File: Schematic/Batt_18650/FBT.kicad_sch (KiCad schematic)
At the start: 17 parts, among them J1 TRRS Connector 3.5, J2 Conn_01x04, SW1 SW_SPDT

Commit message: work on PCBs, logos, and case
did more work on 18650 battery model
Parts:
- removed J2: Conn_01x04, Connector_JST:JST_PH_S4B-PH-K_1x04_P2.00mm_Horizontal, symbol Connector_Generic:Conn_01x04
- added BT-2: Battery anode, Connector_PinHeader_2.54mm:PinHeader_1x01_P2.54mm_Vertical, symbol Connector_Generic:Conn_01x01
- added J2: TRRS Connector 3.5, My_Library:PJ-320A, symbol Connector_Audio:AudioJack4
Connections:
- net ESP32_3V3: now also J2.T
- net GND: now also BT-2.1 (Pin_1), J2.S
- net SCL_1: now also J2.R2
- net SDA_1: now also J2.R1
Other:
- note added: "The GY-27X must be connected to the BMI's 3v3 output so that its logic levels are 3v3. Connecting it to 5v is OK for the GY-273, but the GY-271 will alter i2c logic levels to output 5V, which may hurt the BMI160 Depending on the IMU board, it may not have a 5v tolerant input and instead may need to tap into the 3v3 one. I made the 3v3 input the default one for the sake of versatility."
- note removed: "The GY-27X must be connected to the BMI's 3v3 output so that its logic levels are 3v3. Connecting it to 5v is OK for the GY-273, but the GY-271 will alter i2c logic levels to output 5V, which may hurt the BMI160 Depending on the IMU board, it may not have a 5v tolerant input and instead may need to tap into the 3v3 one."
- moved on the sheet: J1, MCU1

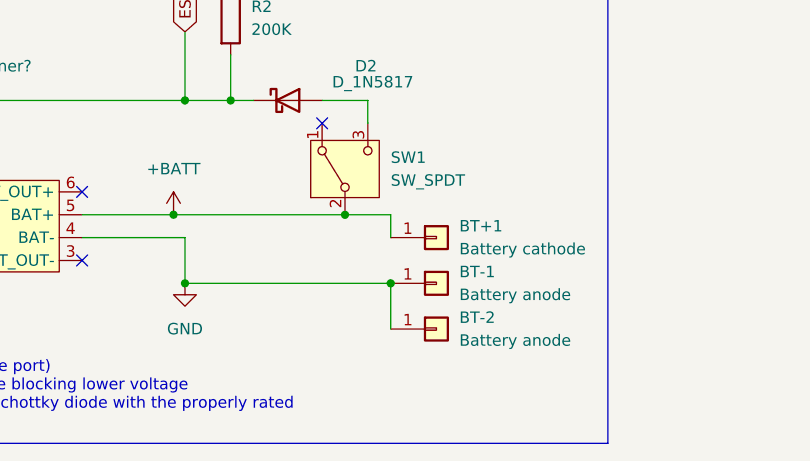
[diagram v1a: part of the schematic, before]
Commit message: Work on 18650 PCB
It's done, but I may re-do this one to flip the ESP32 sideways...
(I then proceeded to work on the sideways version)
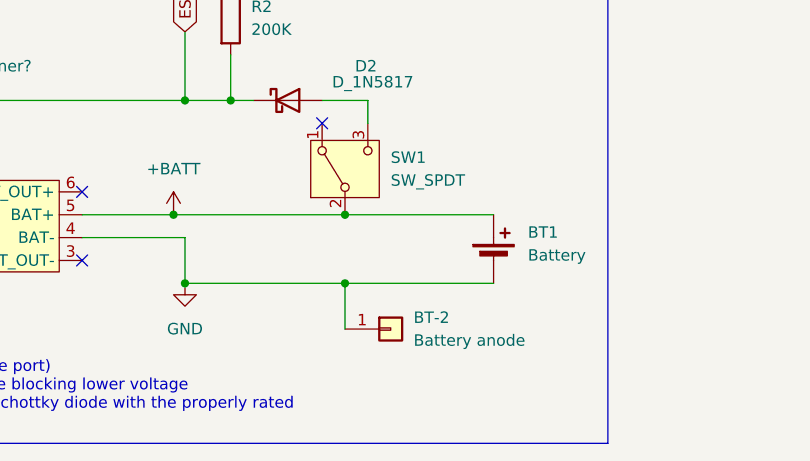
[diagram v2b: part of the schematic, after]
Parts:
- removed BT+1: Battery cathode, Connector_PinHeader_2.54mm:PinHeader_1x01_P2.54mm_Vertical, symbol Connector_Generic:Conn_01x01
- removed BT-1: Battery anode, Connector_PinHeader_2.54mm:PinHeader_1x01_P2.54mm_Vertical, symbol Connector_Generic:Conn_01x01
- added BT1: Battery, Connector_PinHeader_2.54mm:PinHeader_1x02_P2.54mm_Vertical, symbol Device:Battery_Cell
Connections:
- net +BATT: now also BT1.1 (+)
- net GND: now also BT1.2 (-)
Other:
- moved on the sheet: BT-2
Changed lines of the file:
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@@
-	)
-	(junction
-		(at 259.08 140.97)
-		(diameter 0)
-		(color 0 0 0 0)
 	)
 	(junction
@@
 	)
 	(junction
+		(at 254 140.97)
+		(diameter 0)
+		(color 0 0 0 0)
+	)
+	(junction
 		(at 236.22 140.97)
 		(diameter 0)
@@
 	(wire
 		(pts
-			(xy 259.08 135.89) (xy 259.08 133.35)
-		)
-		(stroke
-			(width 0)
-			(type default)
-		)
-	)
-	(wire
-		(pts
 			(xy 261.62 34.29) (xy 261.62 41.91)
 		)
@@
 	(wire
 		(pts
+			(xy 254 140.97) (xy 270.51 140.97)
+		)
+		(stroke
+			(width 0)
+			(type default)
+		)
+	)
+	(wire
+		(pts
 			(xy 227.33 68.58) (xy 229.87 68.58)
 		)
@@
 	(wire
 		(pts
-			(xy 259.08 140.97) (xy 259.08 146.05)
-		)
-		(stroke
-			(width 0)
-			(type default)
-		)
-	)
-	(wire
-		(pts
 			(xy 241.3 106.68) (xy 241.3 107.95)
 		)
@@
 	(wire
 		(pts
-			(xy 254 133.35) (xy 259.08 133.35)
+			(xy 254 133.35) (xy 270.51 133.35)
 		)
 		(stroke
@@
 	(wire
 		(pts
-			(xy 236.22 140.97) (xy 259.08 140.97)
+			(xy 236.22 140.97) (xy 254 140.97)
+		)
+		(stroke
+			(width 0)
+			(type default)
+		)
+	)
+	(wire
+		(pts
+			(xy 254 140.97) (xy 254 146.05)
 		)
 		(stroke
@@
 	(symbol
 		(lib_id "Connector_Generic:Conn_01x01")
-		(at 264.16 146.05 0)
+		(at 259.08 146.05 0)
 		(unit 1)
 		(exclude_from_sim no)
@@
 		(fields_autoplaced yes)
 		(property "Reference" "BT-2"
-			(at 266.7 144.7799 0)
+			(at 261.62 144.7799 0)
 			(effects
 				(font
@@
 		)
 		(property "Value" "Battery anode"
-			(at 266.7 147.3199 0)
+			(at 261.62 147.3199 0)
 			(effects
 				(font
@@
 		)
 		(property "Footprint" "Connector_PinHeader_2.54mm:PinHeader_1x01_P2.54mm_Vertical"
-			(at 264.16 146.05 0)
+			(at 259.08 146.05 0)
 			(effects
 				(font
@@
 		)
 		(property "Datasheet" "~"
-			(at 264.16 146.05 0)
+			(at 259.08 146.05 0)
 			(effects
 				(font
@@
 		)
 		(property "Description" "Generic connector, single row, 01x01, script generated (kicad-library-utils/schlib/autogen/connector/)"
-			(at 264.16 146.05 0)
+			(at 259.08 146.05 0)
 			(effects
 				(font
@@
 				(path "/b59d625c-f89d-4113-8c77-569da8af0dbc"
 					(reference "#PWR01")
+					(unit 1)
+				)
+			)
+		)
+	)
+	(symbol
+		(lib_id "Device:Battery_Cell")
+		(at 270.51 138.43 0)
+		(unit 1)
+		(exclude_from_sim no)
+		(in_bom yes)
+		(on_board yes)
+		(dnp no)
+		(fields_autoplaced yes)
+		(property "Reference" "BT1"
+			(at 274.32 135.3184 0)
+			(effects
+				(font
+					(size 1.27 1.27)
+				)
+				(justify left)
+			)
+		)
+		(property "Value" "Battery"
+			(at 274.32 137.8584 0)
+			(effects
+				(font
+					(size 1.27 1.27)
+				)
+				(justify left)
+			)
+		)
+		(property "Footprint" "Connector_PinHeader_2.54mm:PinHeader_1x02_P2.54mm_Vertical"
+			(at 270.51 136.906 90)
+			(effects
+				(font
+					(size 1.27 1.27)
+				)
+				(hide yes)
+			)
+		)
+		(property "Datasheet" "~"
+			(at 270.51 136.906 90)
+			(effects
+				(font
+					(size 1.27 1.27)
+				)
+				(hide yes)
+			)
+		)
+		(property "Description" "Single-cell battery"
+			(at 270.51 138.43 0)
+			(effects
+				(font
+					(size 1.27 1.27)
+				)
+				(hide yes)
+			)
+		)
+		(pin "2"
+		)
+		(pin "1"
+		)
+		(instances
+			(project "FBT"
+				(path "/b59d625c-f89d-4113-8c77-569da8af0dbc"
+					(reference "BT1")
 					(unit 1)
 				)
@@
 	)
 	(symbol
-		(lib_id "Connector_Generic:Conn_01x01")
-		(at 264.16 135.89 0)
-		(unit 1)
-		(exclude_from_sim no)
-		(in_bom yes)
-		(on_board yes)
-		(dnp no)
-		(fields_autoplaced yes)
-		(property "Reference" "BT+1"
-			(at 266.7 134.6199 0)
-			(effects
-				(font
-					(size 1.27 1.27)
-				)
-				(justify left)
-			)
-		)
-		(property "Value" "Battery cathode"
-			(at 266.7 137.1599 0)
-			(effects
-				(font
-					(size 1.27 1.27)
-				)
-				(justify left)
-			)
-		)
-		(property "Footprint" "Connector_PinHeader_2.54mm:PinHeader_1x01_P2.54mm_Vertical"
-			(at 264.16 135.89 0)
-			(effects
-				(font
-					(size 1.27 1.27)
-				)
-				(hide yes)
-			)
-		)
-		(property "Datasheet" "~"
-			(at 264.16 135.89 0)
-			(effects
-				(font
-					(size 1.27 1.27)
-				)
-				(hide yes)
-			)
-		)
-		(property "Description" "Generic connector, single row, 01x01, script generated (kicad-library-utils/schlib/autogen/connector/)"
-			(at 264.16 135.89 0)
-			(effects
-				(font
-					(size 1.27 1.27)
-				)
-				(hide yes)
-			)
-		)
-		(pin "1"
-		)
-		(instances
-			(project "FBT"
-				(path "/b59d625c-f89d-4113-8c77-569da8af0dbc"
-					(reference "BT+1")
-					(unit 1)
-				)
-			)
-		)
-	)
-	(symbol
 		(lib_id "My_Library:GY-BMI160")
 		(at 240.03 44.45 0)
@@
 					(unit 1)
 				)
-			)
-		)
-	)
-	(symbol
-		(lib_id "Connector_Generic:Conn_01x01")
-		(at 264.16 140.97 0)
-		(unit 1)
-		(exclude_from_sim no)
-		(in_bom yes)
-		(on_board yes)
-		(dnp no)
-		(fields_autoplaced yes)
-		(property "Reference" "BT-1"
-			(at 266.7 139.6999 0)
-			(effects
-				(font
-					(size 1.27 1.27)
-				)
-				(justify left)
-			)
-		)
-		(property "Value" "Battery anode"
-			(at 266.7 142.2399 0)
-			(effects
-				(font
-					(size 1.27 1.27)
-				)
-				(justify left)
-			)
-		)
-		(property "Footprint" "Connector_PinHeader_2.54mm:PinHeader_1x01_P2.54mm_Vertical"
-			(at 264.16 140.97 0)
-			(effects
-				(font
-					(size 1.27 1.27)
-				)
-				(hide yes)
-			)
-		)
-		(property "Datasheet" "~"
-			(at 264.16 140.97 0)
-			(effects
-				(font
-					(size 1.27 1.27)
-				)
-				(hide yes)
-			)
-		)
-		(property "Description" "Generic connector, single row, 01x01, script generated (kicad-library-utils/schlib/autogen/connector/)"
-			(at 264.16 140.97 0)
-			(effects
-				(font
-					(size 1.27 1.27)
-				)
-				(hide yes)
-			)
-		)
-		(pin "1"
-		)
-		(instances
-			(project "FBT"
-				(path "/b59d625c-f89d-4113-8c77-569da8af0dbc"
-					(reference "BT-1")
-					(unit 1)
-				)

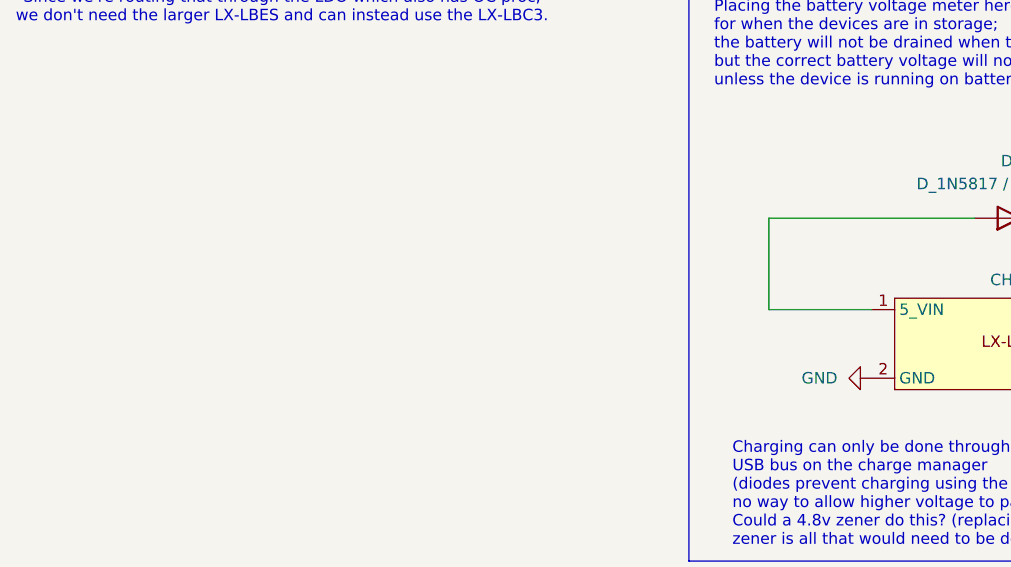
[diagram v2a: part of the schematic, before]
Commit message: work on correcting Ms. Tracker
it has to be a little bit bigger unfortunately...
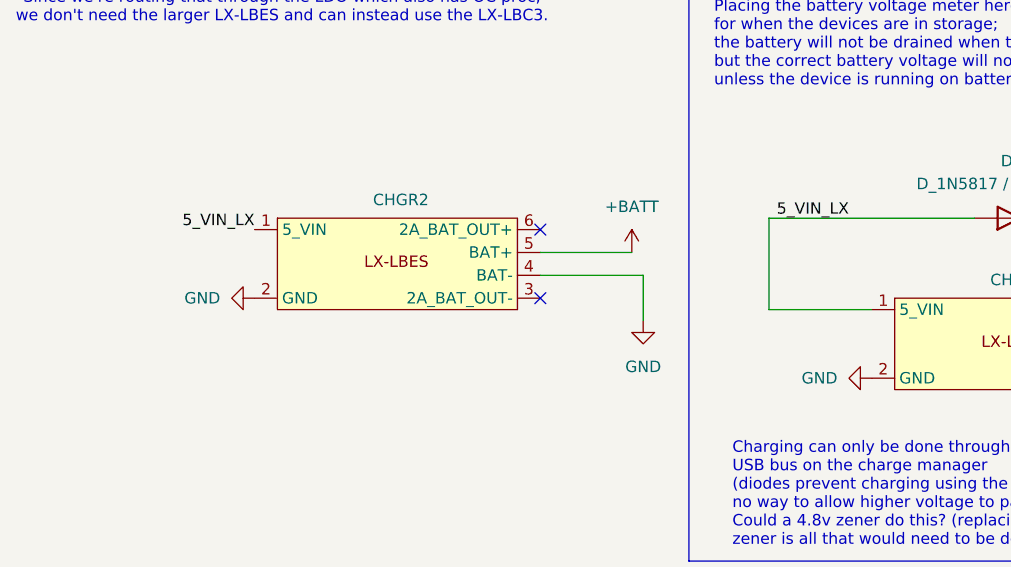
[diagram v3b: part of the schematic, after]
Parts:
- added CHGR2: ~, My_Library:LX-LBES-Big, symbol My_Library:LX-LBES
- MCU1: footprint Espressif:ESP32-C3-SuperMini_PLUS -> Espressif:ESP32-C3-Mini-V1
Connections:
- net +BATT: now also CHGR2.5 (BAT+)
- net GND: now also CHGR2.2 (GND), CHGR2.4 (BAT-)
- net 5_VIN_LX: now reaches CHGR1.1 (5_VIN), D1.2 (A)
- net 5_VIN_LX: now also CHGR2.1 (5_VIN)
- no-connect marks 25 -> 27

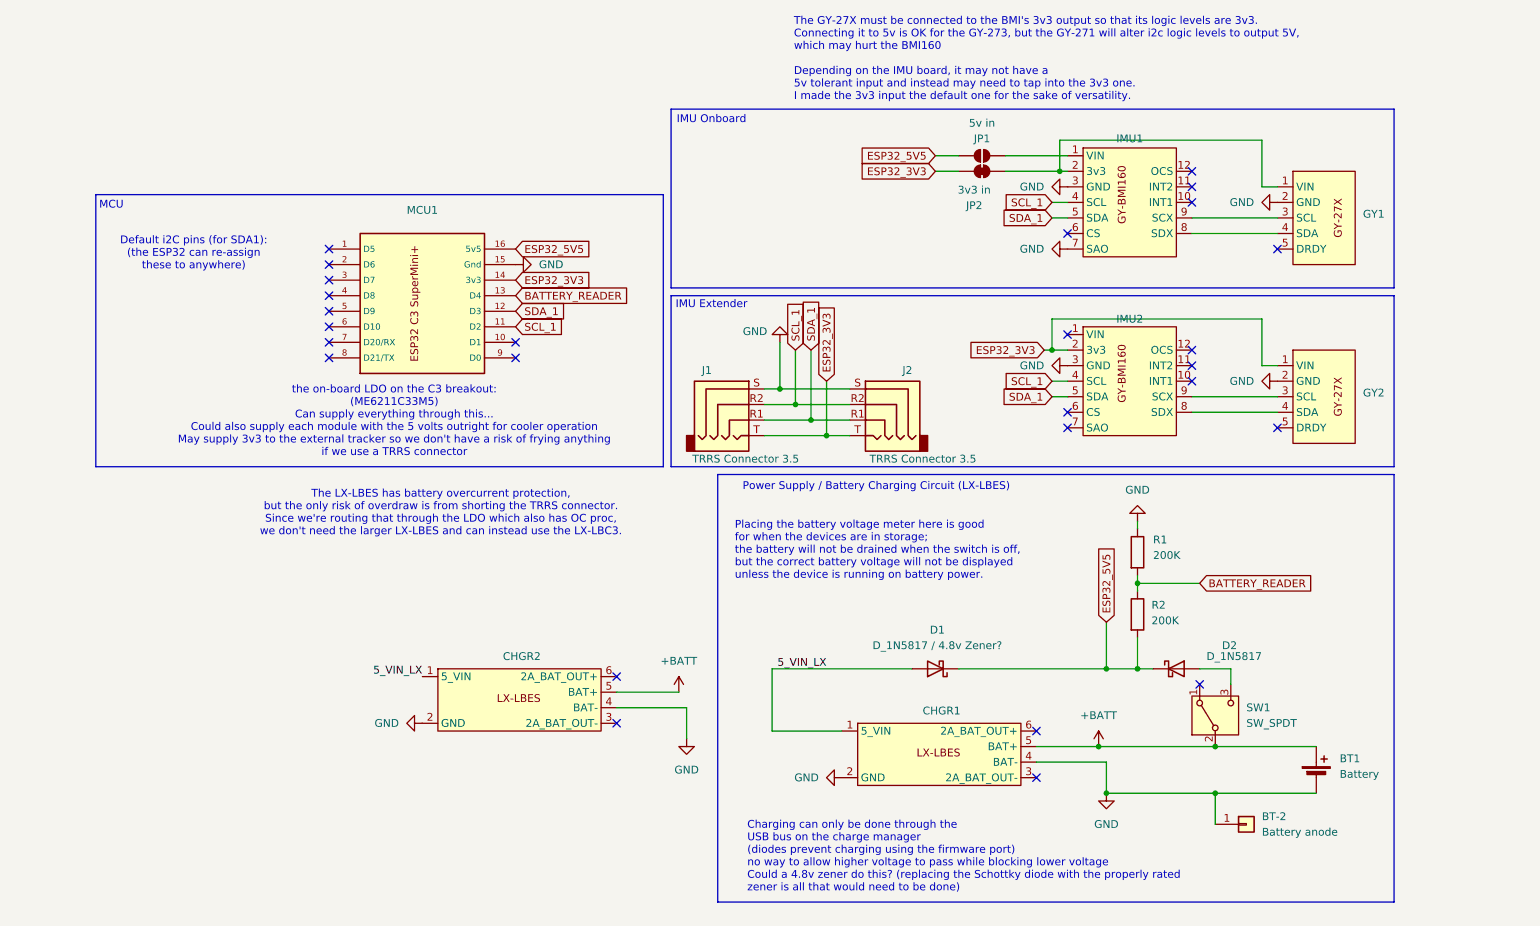
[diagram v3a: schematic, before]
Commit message: Update schematic to v3
Added support for a discrete LDO (HT7333) so we can correct the bodge we did with the original design.
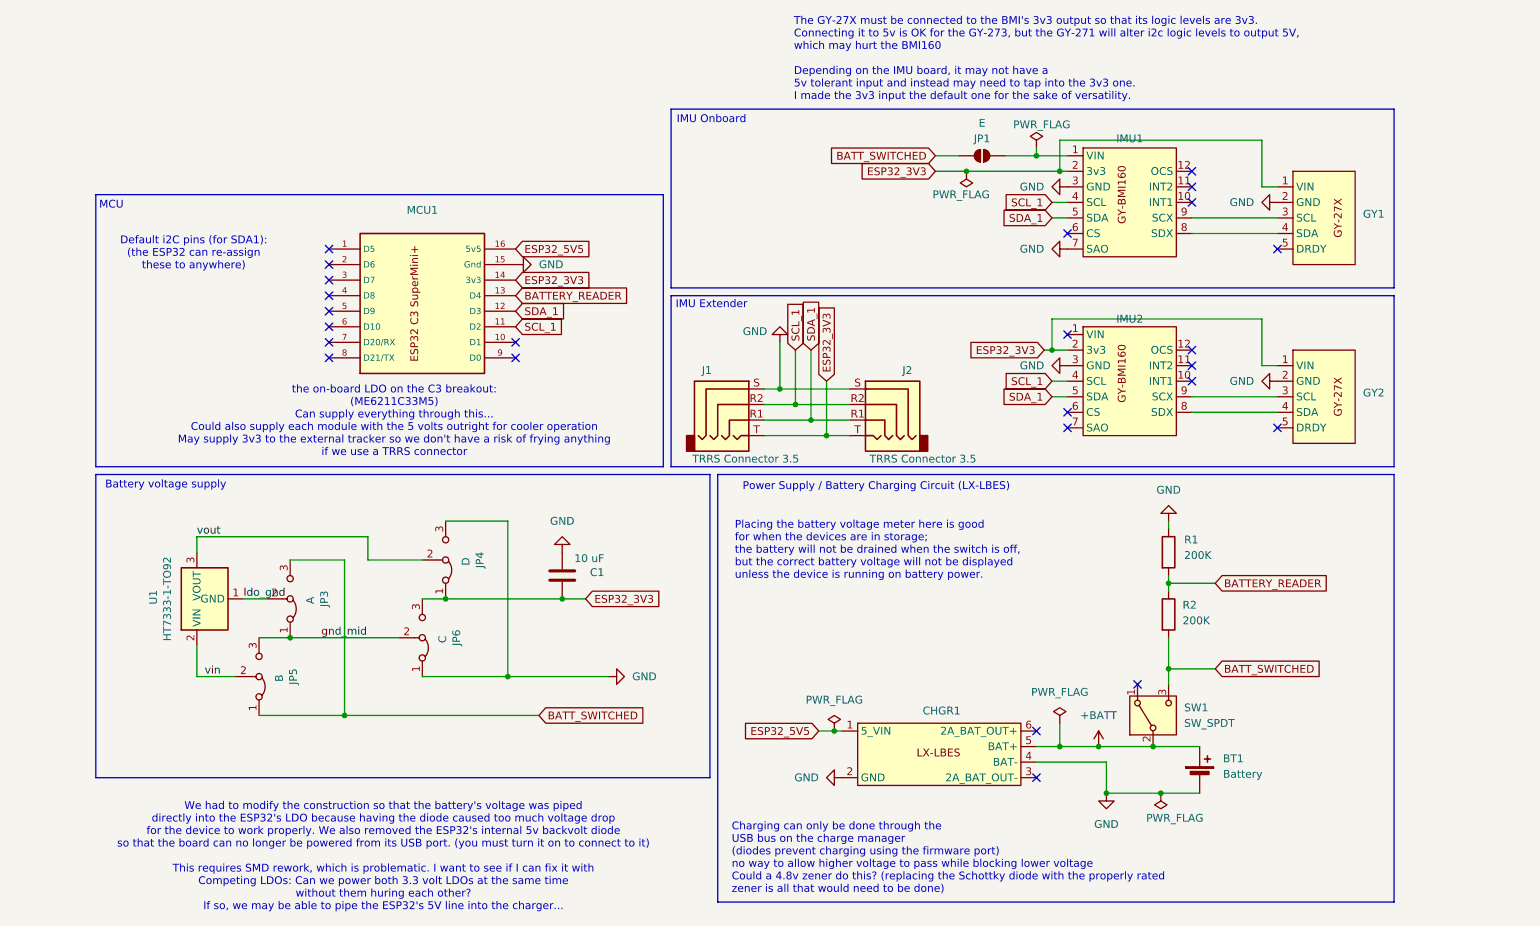
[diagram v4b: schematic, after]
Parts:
- removed BT-2: Battery anode, Connector_PinHeader_2.54mm:PinHeader_1x01_P2.54mm_Vertical, symbol Connector_Generic:Conn_01x01
- removed CHGR2: ~, My_Library:LX-LBES-Big, symbol My_Library:LX-LBES
- removed D1: D_1N5817 / 4.8v Zener?, Diode_THT:D_DO-41_SOD81_P7.62mm_Horizontal, symbol Device:D_Schottky
- removed D2: D_1N5817, Diode_THT:D_DO-41_SOD81_P7.62mm_Horizontal, symbol Device:D_Schottky
- removed JP2: 3v3 in, Jumper:SolderJumper-2_P1.3mm_Bridged_RoundedPad1.0x1.5mm, symbol Jumper:SolderJumper_2_Bridged
- added C1: 10 uF, Capacitor_THT:C_Disc_D5.0mm_W2.5mm_P5.00mm, symbol Device:C
- added JP3: A, Jumper:SolderJumper-3_P1.3mm_Bridged12_RoundedPad1.0x1.5mm_NumberLabels, symbol Jumper:Jumper_3_Bridged12
- added JP4: D, Jumper:SolderJumper-3_P1.3mm_Bridged12_RoundedPad1.0x1.5mm_NumberLabels, symbol Jumper:Jumper_3_Bridged12
- added JP5: B, Jumper:SolderJumper-3_P1.3mm_Bridged12_RoundedPad1.0x1.5mm_NumberLabels, symbol Jumper:Jumper_3_Bridged12
- added JP6: C, Jumper:SolderJumper-3_P1.3mm_Bridged12_RoundedPad1.0x1.5mm_NumberLabels, symbol Jumper:Jumper_3_Bridged12
- added U1: HT7333-1-TO92, Package_TO_SOT_THT:TO-92L_Inline, symbol Regulator_Linear:HT75xx-1-SOT89
- JP1: value 5v in -> E
- MCU1: footprint Espressif:ESP32-C3-Mini-V1 -> Espressif:ESP32-C3-SuperMini_PLUS
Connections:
- net 5_VIN_LX is gone; now on net ESP32_5V5: CHGR1.1 (5_VIN)
- net ESP32_3V3: now also GY1.1 (VIN), IMU1.2 (3v3), C1.1, JP4.1 (A), JP6.3 (B)
- net ESP32_5V5: no longer JP1.2 (B), R2.2
- net GND: now also C1.2, JP4.3 (B), JP6.1 (A)
- net BATT_SWITCHED: now reaches SW1.3 (C)
- net BATT_SWITCHED: now also JP1.2 (B), R2.2, JP3.3 (B), JP5.1 (A)
- new net gnd_mid: JP3.1 (A), JP5.3 (B), JP6.2 (C)
- new net ldo_gnd: JP3.2 (C), U1.1 (GND)
- new net vin: JP5.2 (C), U1.2 (VIN)
- new net vout: JP4.2 (C), U1.3 (VOUT)
- no-connect marks 27 -> 25
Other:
- note added: "Battery voltage supply"
- note added: "We had to modify the construction so that the battery's voltage was piped directly into the ESP32's LDO because having the diode caused too much voltage drop for the device to work properly. We also removed the ESP32's internal 5v backvolt diode so that the board can no longer be powered from its USB port. (you must turn it on to connect to it) This requires SMD rework, which is problematic. I wa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"
- note removed: "The LX-LBES has battery overcurrent protection, but the only risk of overdraw is from shorting the TRRS connector. Since we're routing that through the LDO which also has OC proc, we don't need the larger LX-LBES and can instead use the LX-LBC3."
- moved on the sheet: BT1, R1, R2, SW1
